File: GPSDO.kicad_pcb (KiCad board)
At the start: 2 copper layers, 85 x 85 mm, 102 parts, among them J1 Conn_Coaxial, J10 Conn_Coaxial, J2 Barrel_Jack, J3 PROG, J4 DISP_MODULE, J5 GPS_CONN, J6 Conn_Coaxial, J7 Conn_Coaxial, J8 Conn_Coaxial, J9 Conn_Coaxial, SW1 RESET_BTN, U1 REF3440IDBVR, U10 LM4040AEX3-3.3+T, U11 AVR32DB28x-xSO, U12 AZ1117H-5.0TRG1, U13 AZ1117H-5.0TRG1, U14 74HC390, U15 DS34C87T, U16 MCP6486T-E/OT, U2 74AUC2G04, U3 74AUC2G04, U4 74LVC2G74DP,125, U5 AD5680, U6 NB3N551MN, U7 74LVC1G125SE-7, U8 74LVC1G125SE-7, U9 LTC2050IS8, X1 OC5SC25

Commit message: minor update
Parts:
- moved TP4 1.27 mm to (63.8, 79.4)
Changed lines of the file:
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@@
     (property "Sheetname" "")
     (attr smd)
-    (fp_text reference "R10" (at -1.27 1.651) (layer "F.SilkS")
+    (fp_text reference "R10" (at 0 -1.778) (layer "F.SilkS")
       (effects (font (size 1 1) (thickness 0.15)))
     )
@@
   )
   (footprint "TestPoint:TestPoint_THTPad_2.0x2.0mm_Drill1.0mm" (layer "F.Cu")
-    (at 63.754 78.105)
+    (at 63.754 79.375)
     (descr "THT rectangular pad as test Point, square 2.0mm_Drill1.0mm  side length, hole diameter 1.0mm")
     (tags "test point THT pad rectangle square")

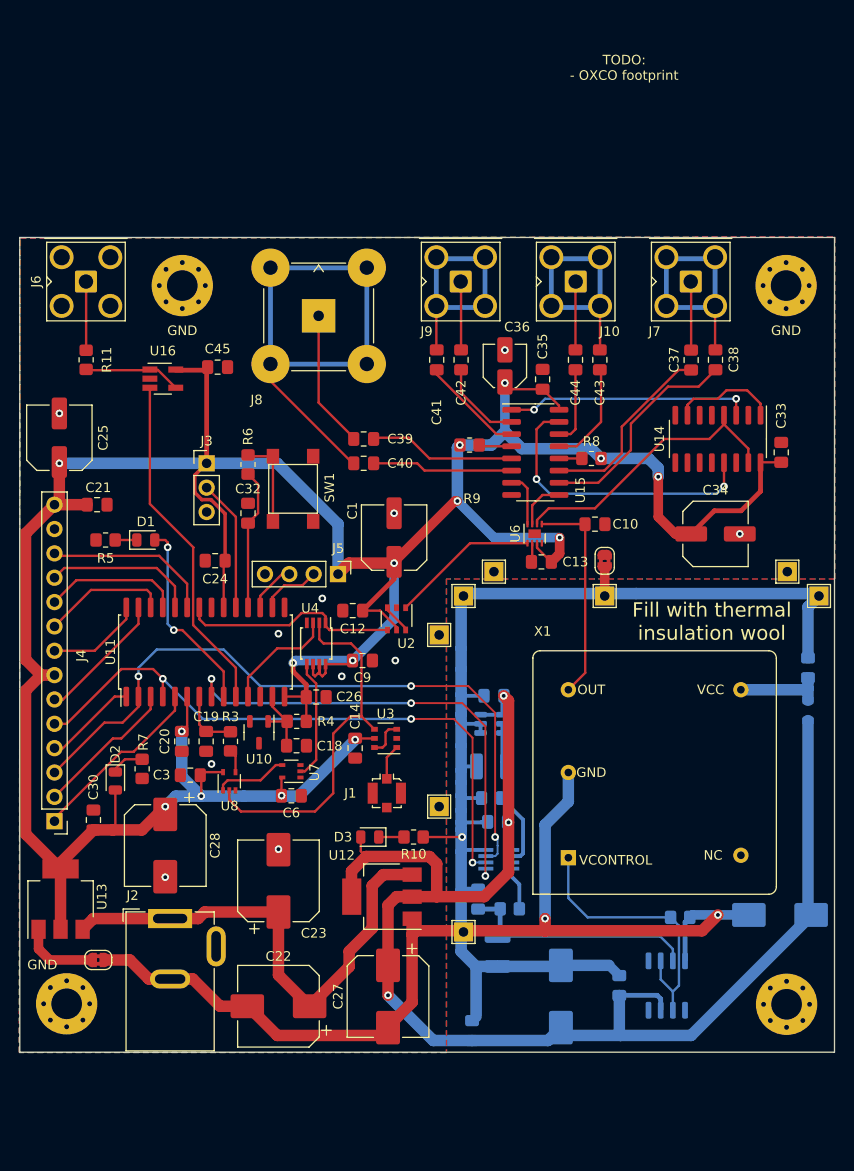
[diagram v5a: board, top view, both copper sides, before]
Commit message: Added a second LED to GPIO & layout cleanup
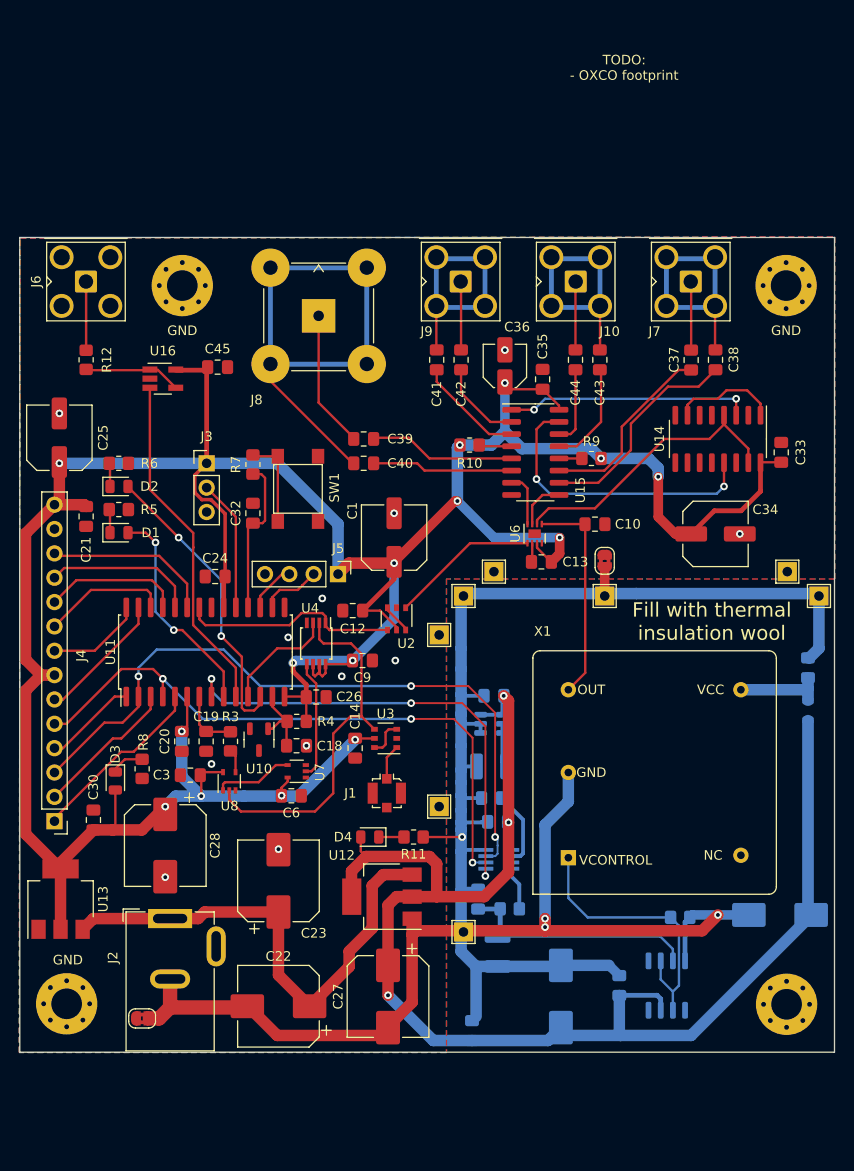
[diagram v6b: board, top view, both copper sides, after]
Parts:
- added D2: LED, LED_SMD:LED_0805_2012Metric, F.Cu at (30.4, 46.0)
- added R6: 270R, Resistor_SMD:R_0805_2012Metric_Pad1.20x1.40mm_HandSolder, F.Cu at (30.3, 43.6)
- moved NT2 7.62 mm to (32.8, 101.5)
- moved R5 3.46 mm to (30.3, 48.4), turned to 180 degrees
- moved D1 2.90 mm to (30.4, 50.8)
- moved C21 1.68 mm to (26.9, 49.1), turned to -90 degrees
- moved C24 1.65 mm to (40.4, 55.4)
- moved U10 0.76 mm to (45.0, 72.4)
- moved U7 0.56 mm to (48.9, 75.7)
- moved C32 0.51 mm to (44.3, 48.8)
- moved R7 0.51 mm to (44.3, 43.7)
- moved SW1 0.51 mm to (49.0, 46.2)
- renumbered D2 to D3, D3 to D4, R9 to R10, R10 to R11, R11 to R12, R6 to R7, R7 to R8, R8 to R9
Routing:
- net /UNUSED: track 0.00 -> 31.1 mm, vias 0 -> 2
- net GND: track 9.74 -> 1.98 mm, vias 11 -> 12
- net Net-(D2-Pad1): track 0.00 -> 2.45 mm
- net Net-(D1-Pad2): track 20.5 -> 22.8 mm
- net GNDA: track 234.9 -> 232.6 mm, vias 3 -> 4
- net /~{RESET}: track 14.8 -> 16.3 mm
- net Net-(U7-Pad4): track 7.61 -> 8.21 mm

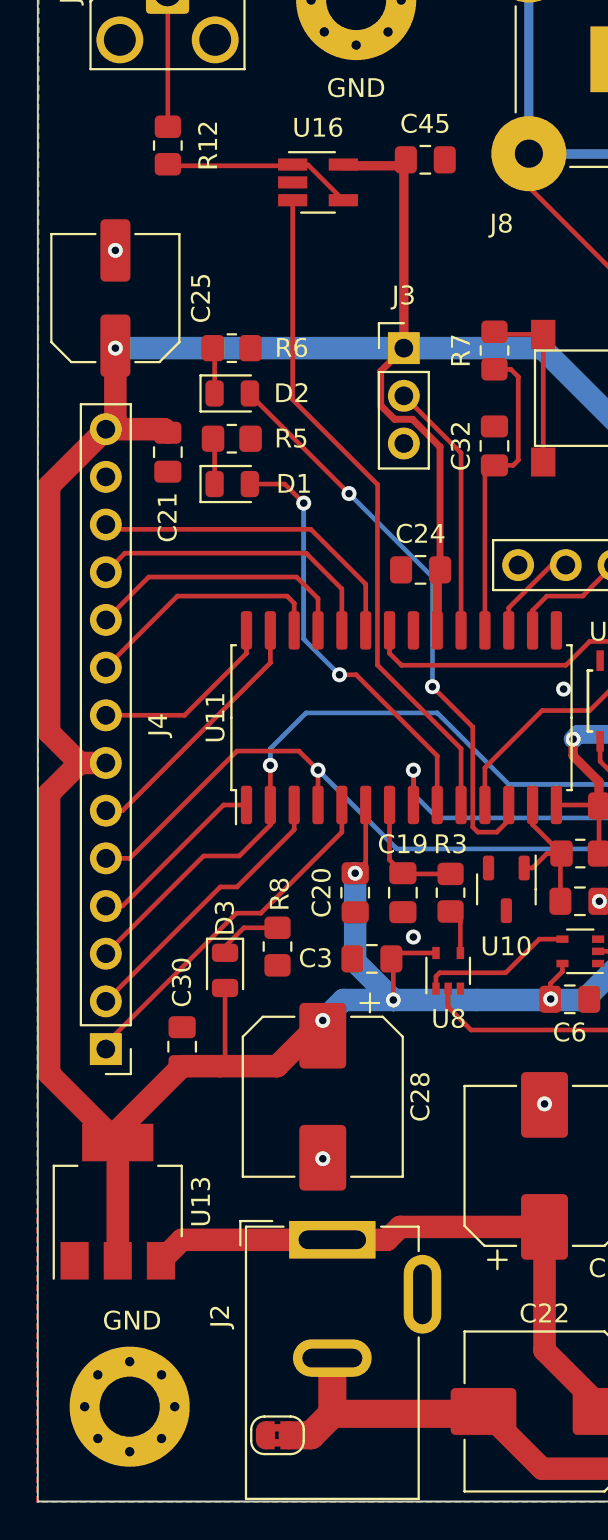
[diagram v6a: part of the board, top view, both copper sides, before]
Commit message: Flipped barrel ground: GND and GNDA, added bottom texts
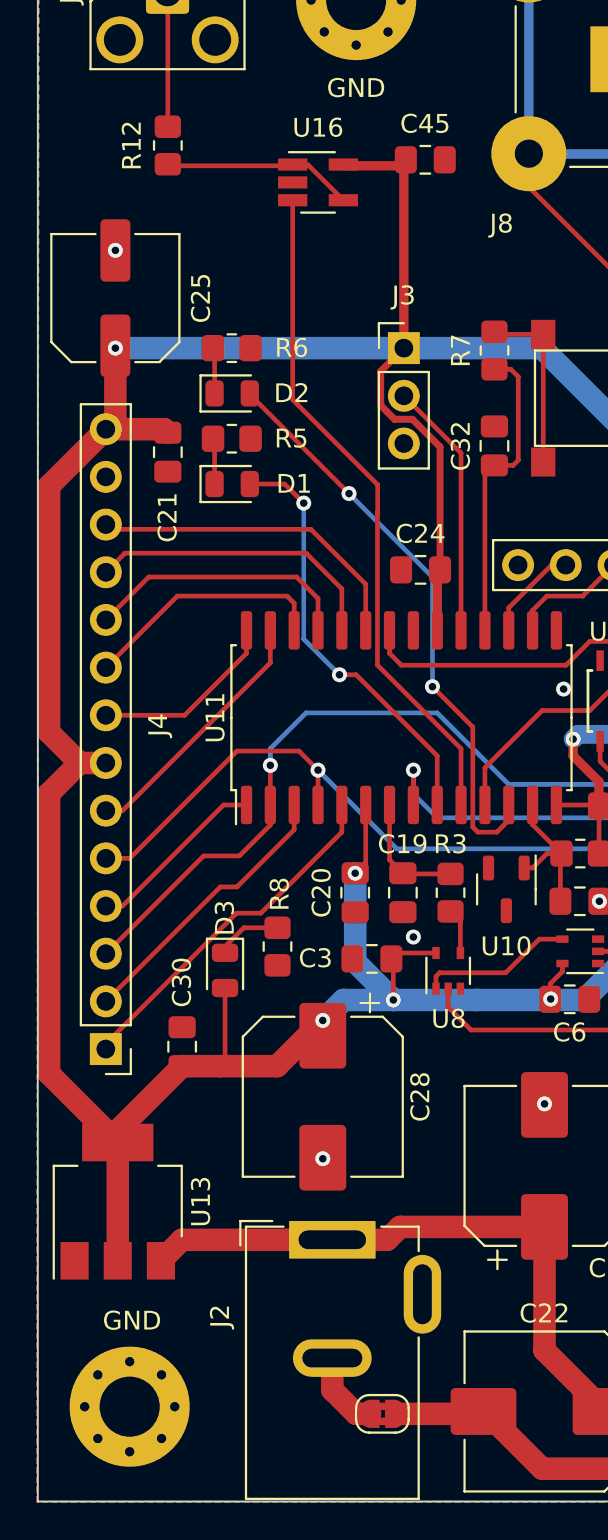
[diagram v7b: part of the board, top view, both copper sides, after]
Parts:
- moved NT2 5.70 mm to (38.4, 100.3), turned to 0 degrees
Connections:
- J2 pad 2: GNDA -> GND
- NT2 pad 1: GNDA -> GND
- NT2 pad 2: GND -> GNDA
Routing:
- net GNDA: track 232.6 -> 223.6 mm
- net GND: track 1.98 -> 6.23 mm
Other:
- board text added: "1 Mc"
- board text added: "1-5VDC 2-GPSRX/uCTX 3-GPSTX/uCRX 4-GND"
- board text added: "10 MC"
- board text added: "10 Mc"
- board text added: "5 Mc"
- board text added: "7VDC - center+"
- board text added: "Custom WF"
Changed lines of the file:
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@@
       (net 49 "/7VIN") (pintype "passive"))
     (pad "2" thru_hole oval locked (at 0 6.3) (size 4.2 2) (drill oval 3.2 1) (layers *.Cu *.Mask)
-      (net 2 "GNDA") (pintype "passive"))
+      (net 6 "GND") (pintype "passive"))
     (pad "3" thru_hole oval locked (at 4.8 2.9) (size 2 4.2) (drill oval 1 3.2) (layers *.Cu *.Mask))
     (model "${KICAD6_3DMODEL_DIR}/Connector_BarrelJack.3dshapes/BarrelJack_GCT_DCJ200-10-A_Horizontal.wrl"
@@
     (property "Sheetname" "")
     (attr smd)
-    (fp_text reference "R12" (at 0 -2.159 90) (layer "F.SilkS")
+    (fp_text reference "R12" (at 0 1.905 90) (layer "F.SilkS")
       (effects (font (size 1 1) (thickness 0.15)))
     )
@@
   )
   (footprint "Jumper:SolderJumper-2_P1.3mm_Bridged2Bar_RoundedPad1.0x1.5mm" (layer "F.Cu")
-    (at 32.766 101.473 180)
+    (at 38.354 100.33)
     (descr "SMD Solder Jumper, 1x1.5mm, rounded Pads, 0.3mm gap, bridged with 2 copper strips")
     (tags "net tie solder jumper bridged")
@@
     (property "exclude_from_bom" "")
     (attr exclude_from_pos_files exclude_from_bom)
-    (fp_text reference "NT2" (at 0 -1.8 180) (layer "F.SilkS") hide
+    (fp_text reference "NT2" (at 0 -1.8) (layer "F.SilkS") hide
       (effects (font (size 1 1) (thickness 0.15)))
     )
-    (fp_text value "NetTie_2" (at 0 1.9 180) (layer "F.Fab")
+    (fp_text value "NetTie_2" (at 0 1.9) (layer "F.Fab")
       (effects (font (size 1 1) (thickness 0.15)))
     )
@@
     (fp_line (start -1.65 -1.25) (end -1.65 1.25) (layer "F.CrtYd") (width 0.05))
     (fp_line (start -1.65 -1.25) (end 1.65 -1.25) (layer "F.CrtYd") (width 0.05))
-    (pad "1" smd custom (at -0.65 0 180) (size 1 0.5) (layers "F.Cu" "F.Mask")
-      (net 2 "GNDA") (pinfunction "1") (pintype "passive") (zone_connect 2)
+    (pad "1" smd custom (at -0.65 0) (size 1 0.5) (layers "F.Cu" "F.Mask")
+      (net 6 "GND") (pinfunction "1") (pintype "passive") (zone_connect 2)
       (options (clearance outline) (anchor rect))
       (primitives
@@
           ) (width 0) (fill yes))
       ))
-    (pad "2" smd custom (at 0.65 0 180) (size 1 0.5) (layers "F.Cu" "F.Mask")
-      (net 6 "GND") (pinfunction "2") (pintype "passive") (zone_connect 2)
+    (pad "2" smd custom (at 0.65 0) (size 1 0.5) (layers "F.Cu" "F.Mask")
+      (net 2 "GNDA") (pinfunction "2") (pintype "passive") (zone_connect 2)
       (options (clearance outline) (anchor rect))
       (primitives
@@
   (gr_line (start 65 56.134) (end 65 104.013) (layer "Dwgs.User") (width 1.6))
   (gr_rect locked (start 20 20) (end 105 105) (layer "Edge.Cuts") (width 0.1) (fill none))
+  (gr_text "5 Mc" (at 77.978 29.972) (layer "B.SilkS")
+    (effects (font (size 1.5 1.5) (thickness 0.3)) (justify mirror))
+  )
+  (gr_text "7VDC - center+" (at 36.322 88.138) (layer "B.SilkS")
+    (effects (font (size 1.5 1.5) (thickness 0.3)) (justify mirror))
+  )
+  (gr_text "1-5VDC\n2-GPSRX/uCTX\n3-GPSTX/uCRX\n4-GND" (at 49.403 53.594 270) (layer "B.SilkS")
+    (effects (font (size 1.2 1.2) (thickness 0.2)) (justify left mirror))
+  )
+  (gr_text "Custom WF" (at 26.797 29.845) (layer "B.SilkS")
+    (effects (font (size 1.5 1.5) (thickness 0.3)) (justify mirror))
+  )
+  (gr_text "1 Mc" (at 66.04 29.972) (layer "B.SilkS")
+    (effects (font (size 1.5 1.5) (thickness 0.3)) (justify mirror))
+  )
+  (gr_text "10 Mc" (at 90.043 29.972) (layer "B.SilkS")
+    (effects (font (size 1.5 1.5) (thickness 0.3)) (justify mirror))
+  )
+  (gr_text "10 MC" (at 51.181 36.322) (layer "B.SilkS")
+    (effects (font (size 1.5 1.5) (thickness 0.3)) (justify mirror))
+  )
   (gr_text "Fill with thermal\ninsulation wool" (at 92.202 60.071) (layer "F.SilkS")
     (effects (font (size 1.5 1.5) (thickness 0.3)))
@@
   (segment (start 62.087 82.55) (end 65.913 82.55) (width 0.25) (layer "F.Cu") (net 2))
   (segment (start 60.935 92.735) (end 60.935 99.797) (width 1.2) (layer "F.Cu") (net 2))
+  (segment (start 43.613 100.33) (end 39.104 100.33) (width 1.2) (layer "F.Cu") (net 2))
   (segment (start 43.613 100.33) (end 43.74 100.203) (width 1.5) (layer "F.Cu") (net 2))
   (segment (start 43.815 100.203) (end 46.863 103.251) (width 1.2) (layer "F.Cu") (net 2))
@@
   (segment (start 57.606 103.251) (end 58.42 102.437) (width 1.2) (layer "F.Cu") (net 2))
   (segment (start 61.341 92.329) (end 60.935 92.735) (width 1.2) (layer "F.Cu") (net 2))
-  (segment (start 35.687 100.33) (end 34.544 101.473) (width 1.5) (layer "F.Cu") (net 2))
   (segment (start 46.863 103.251) (end 57.606 103.251) (width 1.2) (layer "F.Cu") (net 2))
   (segment (start 58.42 102.437) (end 58.42 102.312) (width 1.2) (layer "F.Cu") (net 2))
@@
   (segment (start 74.803 92.329) (end 91.186 92.329) (width 1.2) (layer "F.Cu") (net 2))
   (segment (start 65.913 82.55) (end 66.151 82.788) (width 0.25) (layer "F.Cu") (net 2))
-  (segment (start 34.544 101.473) (end 33.566 101.473) (width 1.5) (layer "F.Cu") (net 2))
-  (segment (start 35.687 97.359) (end 35.687 100.33) (width 1.5) (layer "F.Cu") (net 2))
-  (segment (start 35.687 100.33) (end 43.613 100.33) (width 1.5) (layer "F.Cu") (net 2))
   (segment (start 81.026 54.386) (end 81.026 57.404) (width 1) (layer "F.Cu") (net 2))
   (segment (start 74.803 92.329) (end 61.341 92.329) (width 1.2) (layer "F.Cu") (net 2))
@@
   (segment (start 86.8295 92.9255) (end 69.85 92.9255) (width 0.25) (layer "B.Cu") (net 5))
   (segment (start 73.466 53.7665) (end 73.3845 53.848) (width 0.25) (layer "F.Cu") (net 6))
+  (segment (start 36.957 100.33) (end 37.704 100.33) (width 1.2) (layer "F.Cu") (net 6))
+  (segment (start 35.687 97.359) (end 35.687 99.06) (width 1.2) (layer "F.Cu") (net 6))
   (segment (start 73.466 51.898) (end 73.466 53.7665) (width 0.25) (layer "F.Cu") (net 6))
+  (segment (start 35.687 99.06) (end 36.957 100.33) (width 1.2) (layer "F.Cu") (net 6))
   (via (at 59.182 64.135) (size 0.8) (drill 0.4) (layers "F.Cu" "B.Cu") (free) (net 6))
   (via (at 51.562 57.658) (size 0.8) (drill 0.4) (layers "F.Cu" "B.Cu") (free) (net 6))

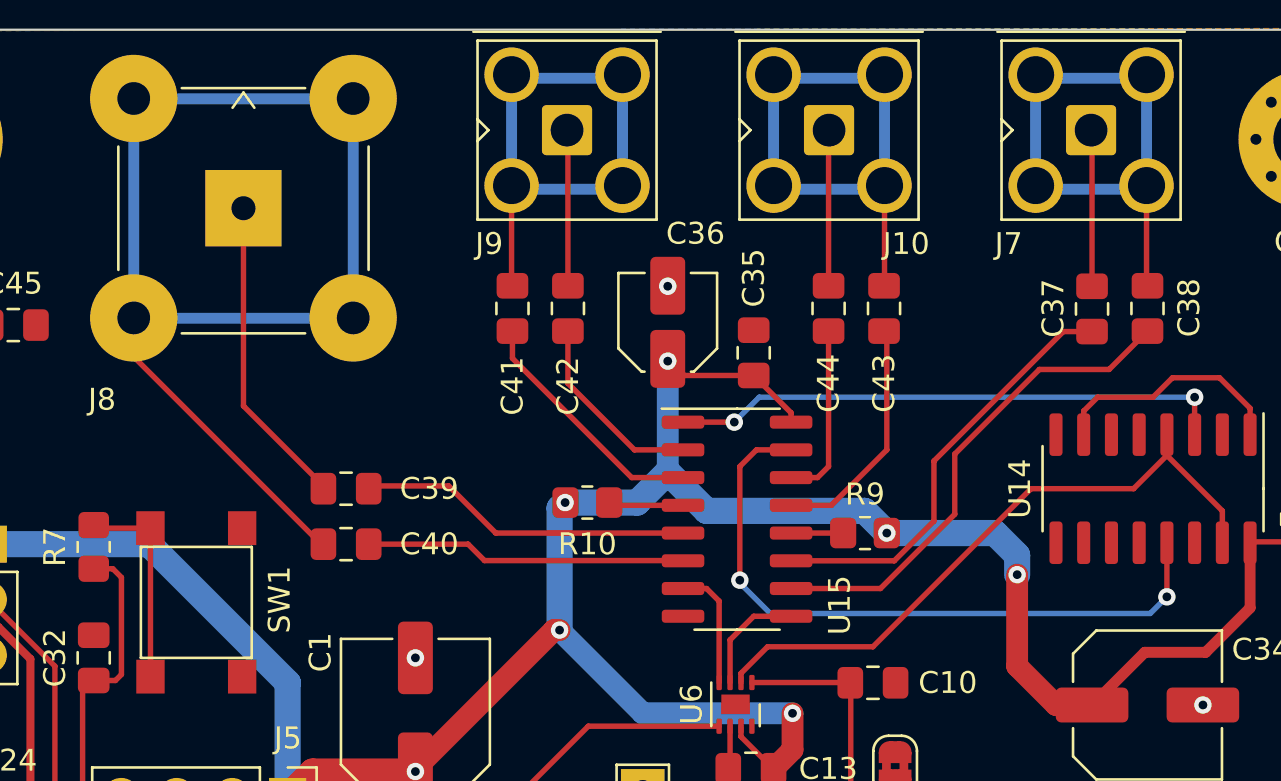
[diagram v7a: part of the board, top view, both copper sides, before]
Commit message: Differential pairs leaving the drivers are equal in length
difference is in the order 0.01 mm
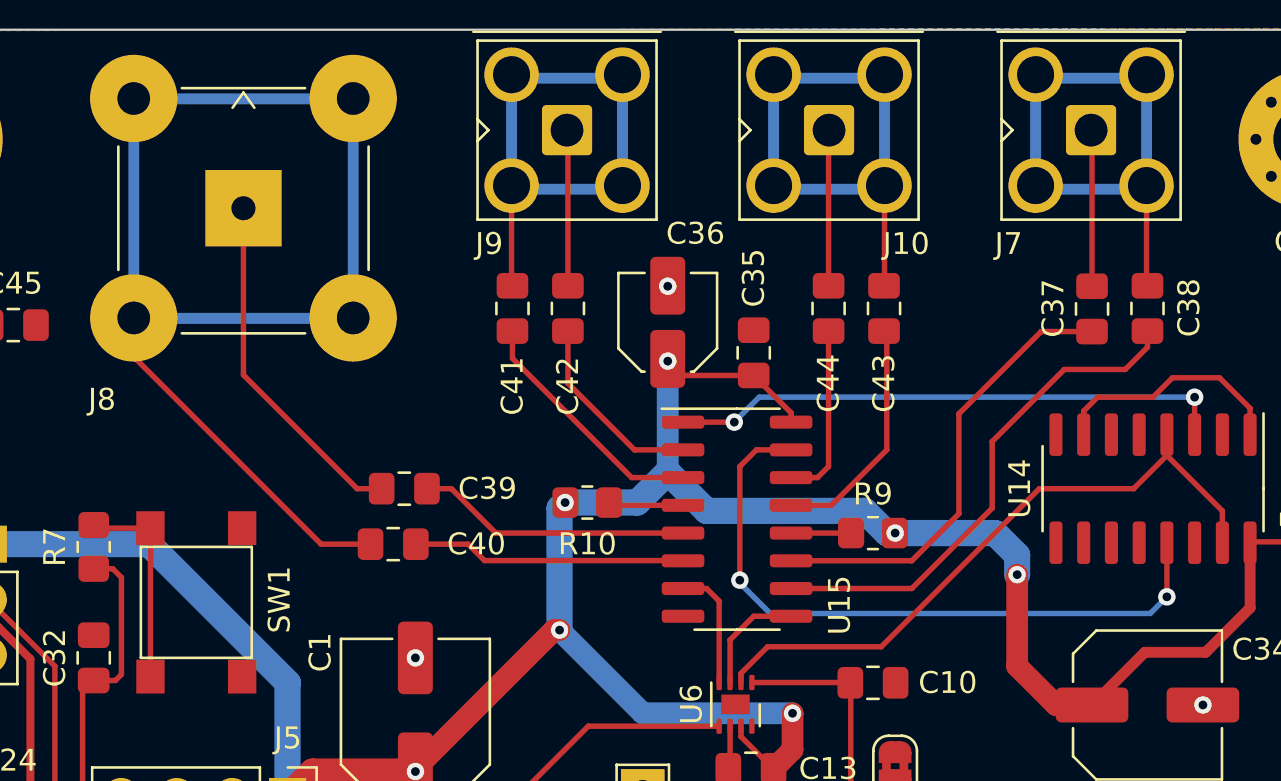
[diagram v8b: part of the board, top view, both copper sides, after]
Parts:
- moved C39 2.67 mm to (58.5, 41.0)
- moved C40 2.16 mm to (58.0, 43.6)
- moved R9 0.37 mm to (80.0, 43.1)
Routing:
- net Net-(C39-Pad1): track 15.3 -> 12.6 mm
- net Net-(C40-Pad1): track 14.7 -> 12.6 mm
- net Net-(C40-Pad2): track 54.2 -> 56.4 mm
- net Net-(C39-Pad2): track 14.2 -> 16.1 mm
- net Net-(C37-Pad1): track 19.7 -> 20.8 mm
- net Net-(C38-Pad1): track 22.8 -> 23.4 mm
